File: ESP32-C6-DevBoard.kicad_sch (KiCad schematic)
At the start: 44 parts, among them J1 USB_C_Receptacle_USB2.0_16P, J2 Conn_01x10_Pin, J3 Conn_01x10_Pin, J4 USB_C_Receptacle_USB2.0_16P, Q1 BC847, Q2 BC847, SW1 SW_Push_Dual, SW2 SW_Push_Dual, U1 ESP32-C6-MINI-1, U2 CP2104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

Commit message: First version done without autorouter.
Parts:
- removed J2, J3: Conn_01x10_Pin, Connector_PinHeader_2.54mm:PinHeader_1x10_P2.54mm_Vertical, symbol Connector:Conn_01x10_Pin
- removed SW1, SW2: SW_Push_Dual, TS04_66_55_BK_260_SMT:SW_TS04-66-55-BK-260-SMT, symbol Switch:SW_Push_Dual
- removed U4, U5: USBLC6-2SC6, Package_TO_SOT_SMD:SOT-23-6, symbol Power_Protection:USBLC6-2SC6
- added D10, D11, D12, D6, D8, D9: SD05_SOD323, Diode_SMD:D_SOD-323, symbol Diode:SD05_SOD323
- added J2: Conn_01x02_Pin, Connector_PinHeader_2.54mm:PinHeader_1x02_P2.54mm_Vertical, symbol Connector:Conn_01x02_Pin
- added J5, J6: Conn_01x16_Pin, Connector_PinHeader_2.54mm:PinHeader_1x16_P2.54mm_Vertical, symbol Connector:Conn_01x16_Pin
- added S1, S2: TS-1088-AR02016, TS-1088-AR02016:SW_TS-1088-AR02016, symbol TS-1088-AR02016:TS-1088-AR02016
- C5: value 0.1uF -> 1.0uF
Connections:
- net CHIP_PU: now also S1.2
- net EIO0: now also S2.2
- net EIO1: now also J6.4 (Pin_4)
- net EIO14: now also J5.9 (Pin_9)
- net EIO15: now also J5.10 (Pin_10)
- net EIO18: now also J5.11 (Pin_11)
- net EIO19: now also J5.12 (Pin_12)
- net EIO2: now also J6.14 (Pin_14)
- net EIO20: now also J5.13 (Pin_13)
- net EIO21: now also J5.14 (Pin_14)
- net EIO22: now also J5.15 (Pin_15)
- net EIO23: now also J5.16 (Pin_16)
- net EIO3: now also J6.7 (Pin_7)
- net EIO4: now also J6.6 (Pin_6)
- net EIO5: now also J6.5 (Pin_5)
- net EIO6: now also J5.7 (Pin_7)
- net EIO7: now also J5.8 (Pin_8)
- net GND: now also D10.1 (A1), D11.1 (A1), D12.1 (A1), D6.1 (A1), D8.1 (A1), D9.1 (A1), J6.1 (Pin_1), S1.1, S2.1
- net USB1_N: now also J1.A7 (D-), J1.B7 (D-), D11.2 (A2)
- net USB1_P: now also J1.A6 (D+), J1.B6 (D+), D12.2 (A2)
- net USB2_N: now also J4.A7 (D-), J4.B7 (D-), D9.2 (A2)
- net USB2_P: now also J4.A6 (D+), J4.B6 (D+), D8.2 (A2)
- net DTR: now reaches Q2.3 (C), R11.2, U2.23 (~{DTR})
- net RTS: now reaches Q1.3 (C), R14.1, U2.19 (~{RTS})
- net 3V3 renamed PWR_3V3
- net PWR_3V3: now also J2.1 (Pin_1), J6.3 (Pin_3); no longer C2.1, R3.1, R5.1, U3.1 (OUT)
- net USB1_VBUS renamed PWR_USB1_VBUS
- net PWR_USB1_VBUS: now also D10.2 (A2)
- net USB2_VBUS renamed PWR_USB2_VBUS
- net PWR_USB2_VBUS: now also D6.2 (A2)
- net USB_5V renamed PWR_5V
- net PWR_5V: now also J6.2 (Pin_2)
- new net: C2.1, J2.2 (Pin_2), R3.1, R5.1, U3.1 (OUT)
- no-connect marks 14 -> 29
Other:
- note removed: "Pin grid"
- moved on the sheet: D3

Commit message: Updated silk screen and corrected component error
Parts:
- C1, C2, C7, C8: Part_No TORCH CT4G-1206-X5R-16V-10μF-K -> Samsung Electro-Mechanics CL10A106MA8NRNC
- C5: Part_No 0603B104K500NT -> Samsung Electro-Mechanics CL10A105KB8NNNC
- D10, D11, D12, D6, D8, D9: Part_No (none) -> MDD(Microdiode Semiconductor) SD05
- J2: Part_No (none) -> Ckmtw(Shenzhen Cankemeng) B-2100S02P-A110
- J5, J6: Part_No (none) -> HanElectricity 2541WV-16P
- S1, S2: Part_No (none) -> XUNPU TS-1088-AR02016

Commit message: Updated BOM
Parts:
- C1, C2, C7, C8: LCSC Part Name (none) -> C96446
- C3: LCSC Part Name (none) -> C19666
- C4, C6, C9: LCSC Part Name (none) -> C30926; Part_No 0603B104K500NT -> FH (Guangdong Fenghua Advanced Tech) 0603B104K500NT
- C5: LCSC Part Name (none) -> C15849
- D1: LCSC Part Name (none) -> C125123
- D10, D11, D12, D6, D8, D9: LCSC Part Name (none) -> C502527
- D2, D3: LCSC Part Name (none) -> C191023
- D4: LCSC Part Name (none) -> C125103
- D5, D7: LCSC Part Name (none) -> C12065
- J1, J4: LCSC Part Name (none) -> C2765186
- J2: LCSC Part Name (none) -> C124375
- J5, J6: LCSC Part Name (none) -> C25503134
- Q1, Q2: LCSC Part Name (none) -> C57668
- R1, R2, R7, R8: LCSC Part Name (none) -> C23186
- R10, R13, R15, R17, R5, R9: LCSC Part Name (none) -> C23197
- R11, R14, R6: LCSC Part Name (none) -> C25804
- R12: LCSC Part Name (none) -> C23179
- R3: LCSC Part Name (none) -> C22935
- R4: LCSC Part Name (none) -> C25811
- S1, S2: LCSC Part Name (none) -> C720477
- U1: LCSC Part Name (none) -> C5736265
- U2: LCSC Part Name (none) -> C47742
- U3: LCSC Part Name (none) -> C2876308
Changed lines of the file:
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@@
 			)
 		)
-		(property "LCSC Part Name" ""
+		(property "LCSC Part Name" "C125103"
 			(at 66.04 36.83 0)
 			(effects
@@
 			)
 		)
-		(property "LCSC Part Name" ""
+		(property "LCSC Part Name" "C12065"
 			(at 38.1 168.91 0)
 			(effects
@@
 			)
 		)
-		(property "LCSC Part Name" ""
+		(property "LCSC Part Name" "C720477"
 			(at 295.91 64.77 0)
 			(effects
@@
 			)
 		)
-		(property "LCSC Part Name" ""
+		(property "LCSC Part Name" "C25804"
 			(at 227.33 48.26 0)
 			(effects
@@
 			)
 		)
-		(property "Part_No" "0603B104K500NT"
+		(property "Part_No" "FH (Guangdong Fenghua Advanced Tech) 0603B104K500NT"
 			(at 368.3 26.67 0)
 			(effects
@@
 			)
 		)
-		(property "LCSC Part Name" ""
+		(property "LCSC Part Name" "C30926"
 			(at 368.3 26.67 0)
 			(effects
@@
 			)
 		)
-		(property "LCSC Part Name" ""
+		(property "LCSC Part Name" "C502527"
 			(at 63.5 54.61 0)
 			(effects
@@
 			)
 		)
-		(property "LCSC Part Name" ""
+		(property "LCSC Part Name" "C125123"
 			(at 91.44 168.91 0)
 			(effects
@@
 			)
 		)
-		(property "LCSC Part Name" ""
+		(property "LCSC Part Name" "C23197"
 			(at 195.58 38.1 0)
 			(effects
@@
 			)
 		)
-		(property "LCSC Part Name" ""
+		(property "LCSC Part Name" "C720477"
 			(at 295.91 43.18 0)
 			(effects
@@
 			)
 		)
-		(property "LCSC Part Name" ""
+		(property "LCSC Part Name" "C15849"
 			(at 303.53 46.99 0)
 			(effects
@@
 			)
 		)
-		(property "Part_No" "0603B104K500NT"
+		(property "Part_No" "FH (Guangdong Fenghua Advanced Tech) 0603B104K500NT"
 			(at 316.23 69.85 0)
 			(effects
@@
 			)
 		)
-		(property "LCSC Part Name" ""
+		(property "LCSC Part Name" "C30926"
 			(at 316.23 69.85 0)
 			(effects
@@
 			)
 		)
-		(property "LCSC Part Name" ""
+		(property "LCSC Part Name" "C25804"
 			(at 303.53 26.67 0)
 			(effects
@@
 			)
 		)
-		(property "LCSC Part Name" ""
+		(property "LCSC Part Name" "C96446"
 			(at 78.74 163.83 0)
 			(effects
@@
 			)
 		)
-		(property "LCSC Part Name" ""
+		(property "LCSC Part Name" "C57668"
 			(at 234.95 72.39 0)
 			(effects
@@
 			)
 		)
-		(property "LCSC Part Name" ""
+		(property "LCSC Part Name" "C22935"
 			(at 66.04 161.29 0)
 			(effects
@@
 			)
 		)
-		(property "LCSC Part Name" ""
+		(property "LCSC Part Name" "C23197"
 			(at 66.04 29.21 0)
 			(effects
@@
 			)
 		)
-		(property "LCSC Part Name" ""
+		(property "LCSC Part Name" "C5736265"
 			(at 350.52 63.5 0)
 			(effects
@@
 			)
 		)
-		(property "LCSC Part Name" ""
+		(property "LCSC Part Name" "C502527"
 			(at 74.93 38.1 0)
 			(effects
@@
 			)
 		)
-		(property "LCSC Part Name" ""
+		(property "LCSC Part Name" "C23186"
 			(at 58.42 36.83 0)
 			(effects
@@
 			)
 		)
-		(property "LCSC Part Name" ""
+		(property "LCSC Part Name" "C23197"
 			(at 38.1 161.29 0)
 			(effects
@@
 			)
 		)
-		(property "LCSC Part Name" ""
+		(property "LCSC Part Name" "C57668"
 			(at 237.49 48.26 0)
 			(effects
@@
 			)
 		)
-		(property "LCSC Part Name" ""
+		(property "LCSC Part Name" "C2876308"
 			(at 48.26 160.02 0)
 			(effects
@@
 			)
 		)
-		(property "LCSC Part Name" ""
+		(property "LCSC Part Name" "C124375"
 			(at 97.79 152.4 0)
 			(effects
@@
 			)
 		)
-		(property "LCSC Part Name" ""
+		(property "LCSC Part Name" "C23197"
 			(at 195.58 35.56 0)
 			(effects
@@
 			)
 		)
-		(property "LCSC Part Name" ""
+		(property "LCSC Part Name" "C12065"
 			(at 63.5 100.33 0)
 			(effects
@@
 			)
 		)
-		(property "LCSC Part Name" ""
+		(property "LCSC Part Name" "C191023"
 			(at 78.74 88.9 0)
 			(effects
@@
 			)
 		)
-		(property "LCSC Part Name" ""
+		(property "LCSC Part Name" "C502527"
 			(at 74.93 102.87 0)
 			(effects
@@
 			)
 		)
-		(property "Part_No" "0603B104K500NT"
+		(property "Part_No" "FH (Guangdong Fenghua Advanced Tech) 0603B104K500NT"
 			(at 144.78 30.48 0)
 			(effects
@@
 			)
 		)
-		(property "LCSC Part Name" ""
+		(property "LCSC Part Name" "C30926"
 			(at 144.78 30.48 0)
 			(effects
@@
 			)
 		)
-		(property "LCSC Part Name" ""
+		(property "LCSC Part Name" "C2765186"
 			(at 39.37 46.99 0)
 			(effects
@@
 			)
 		)
-		(property "LCSC Part Name" ""
+		(property "LCSC Part Name" "C502527"
 			(at 68.58 120.65 0)
 			(effects
@@
 			)
 		)
-		(property "LCSC Part Name" ""
+		(property "LCSC Part Name" "C23197"
 			(at 91.44 162.56 0)
 			(effects
@@
 			)
 		)
-		(property "LCSC Part Name" ""
+		(property "LCSC Part Name" "C25811"
 			(at 66.04 168.91 0)
 			(effects
@@
 			)
 		)
-		(property "LCSC Part Name" ""
+		(property "LCSC Part Name" "C23197"
 			(at 63.5 92.71 0)
 			(effects
@@
 			)
 		)
-		(property "LCSC Part Name" ""
+		(property "LCSC Part Name" "C23186"
 			(at 58.42 40.64 0)
 			(effects
@@
 			)
 		)
-		(property "LCSC Part Name" ""
+		(property "LCSC Part Name" "C96446"
 			(at 356.87 26.67 0)
 			(effects
@@
 			)
 		)
-		(property "LCSC Part Name" ""
+		(property "LCSC Part Name" "C2765186"
 			(at 33.02 113.03 0)
 			(effects
@@
 			)
 		)
-		(property "LCSC Part Name" ""
+		(property "LCSC Part Name" "C502527"
 			(at 59.69 120.65 0)
 			(effects
@@
 			)
 		)
-		(property "LCSC Part Name" ""
+		(property "LCSC Part Name" "C23186"
 			(at 57.15 105.41 0)
 			(effects
@@
 			)
 		)
-		(property "LCSC Part Name" ""
+		(property "LCSC Part Name" "C23179"
 			(at 160.02 31.75 0)
 			(effects
@@
 			)
 		)
-		(property "LCSC Part Name" ""
+		(property "LCSC Part Name" "C191023"
 			(at 80.01 31.75 0)
 			(effects
@@
 			)
 		)
-		(property "LCSC Part Name" ""
+		(property "LCSC Part Name" "C19666"
 			(at 157.48 82.55 0)
 			(effects
@@
 			)
 		)
-		(property "LCSC Part Name" ""
+		(property "LCSC Part Name" "C47742"
 			(at 176.53 58.42 0)
 			(effects
@@
 			)
 		)
-		(property "LCSC Part Name" ""
+		(property "LCSC Part Name" "C96446"
 			(at 152.4 30.48 0)
 			(effects
@@
 			)
 		)
-		(property "LCSC Part Name" ""
+		(property "LCSC Part Name" "C96446"
 			(at 33.02 163.83 0)
 			(effects
@@
 			)
 		)
-		(property "LCSC Part Name" ""
+		(property "LCSC Part Name" "C25804"
 			(at 226.06 72.39 0)
 			(effects
@@
 			)
 		)
-		(property "LCSC Part Name" ""
+		(property "LCSC Part Name" "C25503134"
 			(at 203.2 144.78 0)
 			(effects
@@
 			)
 		)
-		(property "LCSC Part Name" ""
+		(property "LCSC Part Name" "C25503134"
 			(at 228.6 144.78 0)
 			(effects
@@
 			)
 		)
-		(property "LCSC Part Name" ""
+		(property "LCSC Part Name" "C23186"
 			(at 57.15 100.33 0)
 			(effects
@@
 			)
 		)
-		(property "LCSC Part Name" ""
+		(property "LCSC Part Name" "C502527"
 			(at 73.66 54.61 0)
 			(effects

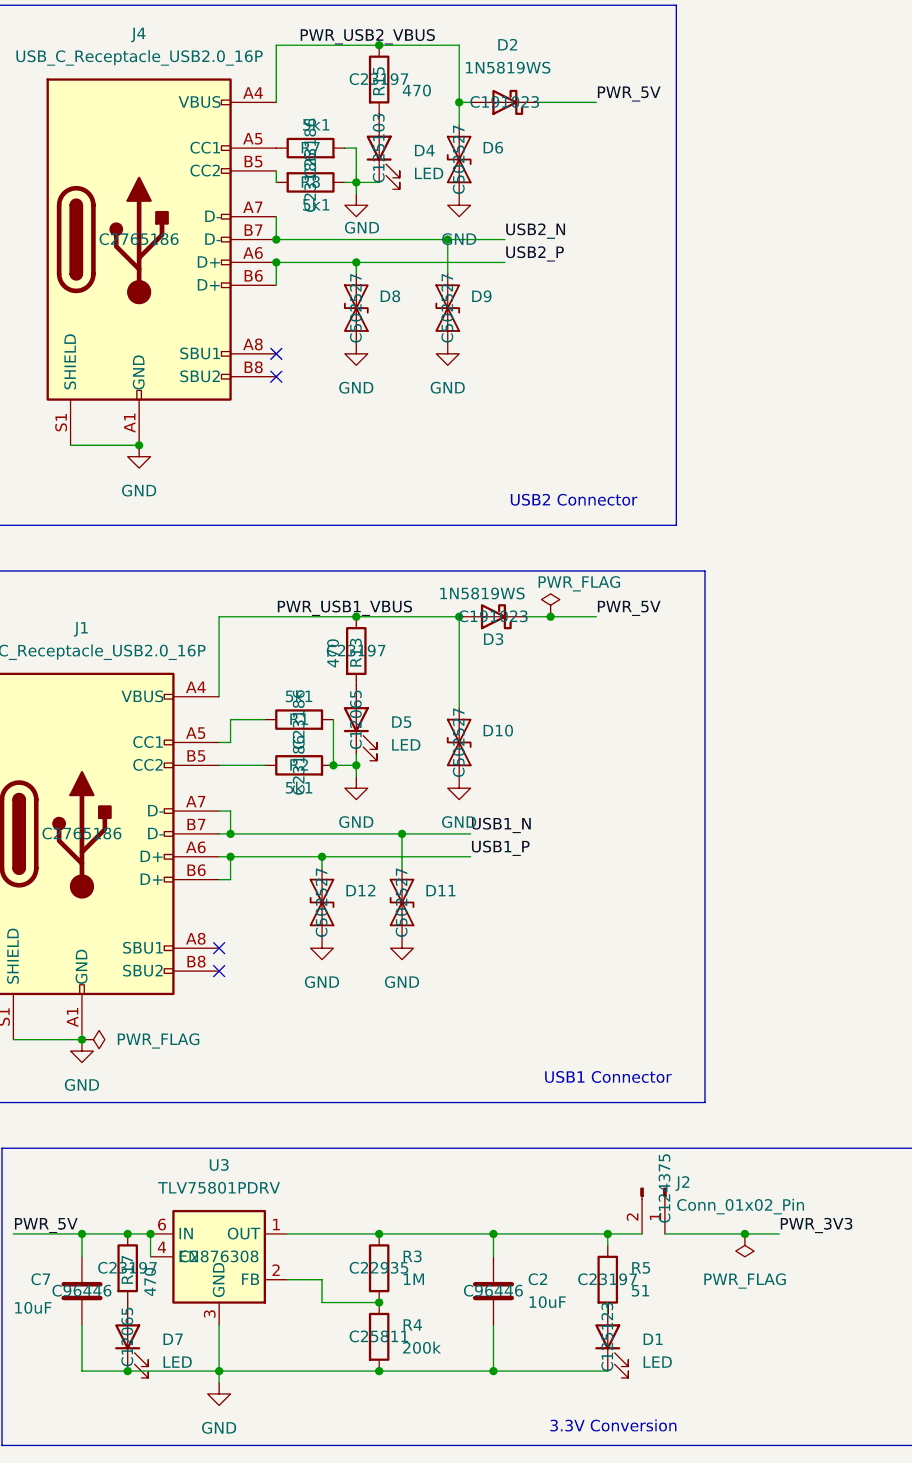
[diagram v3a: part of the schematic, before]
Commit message: Updated BOM using Buoni kicad-jlcpcb-tools
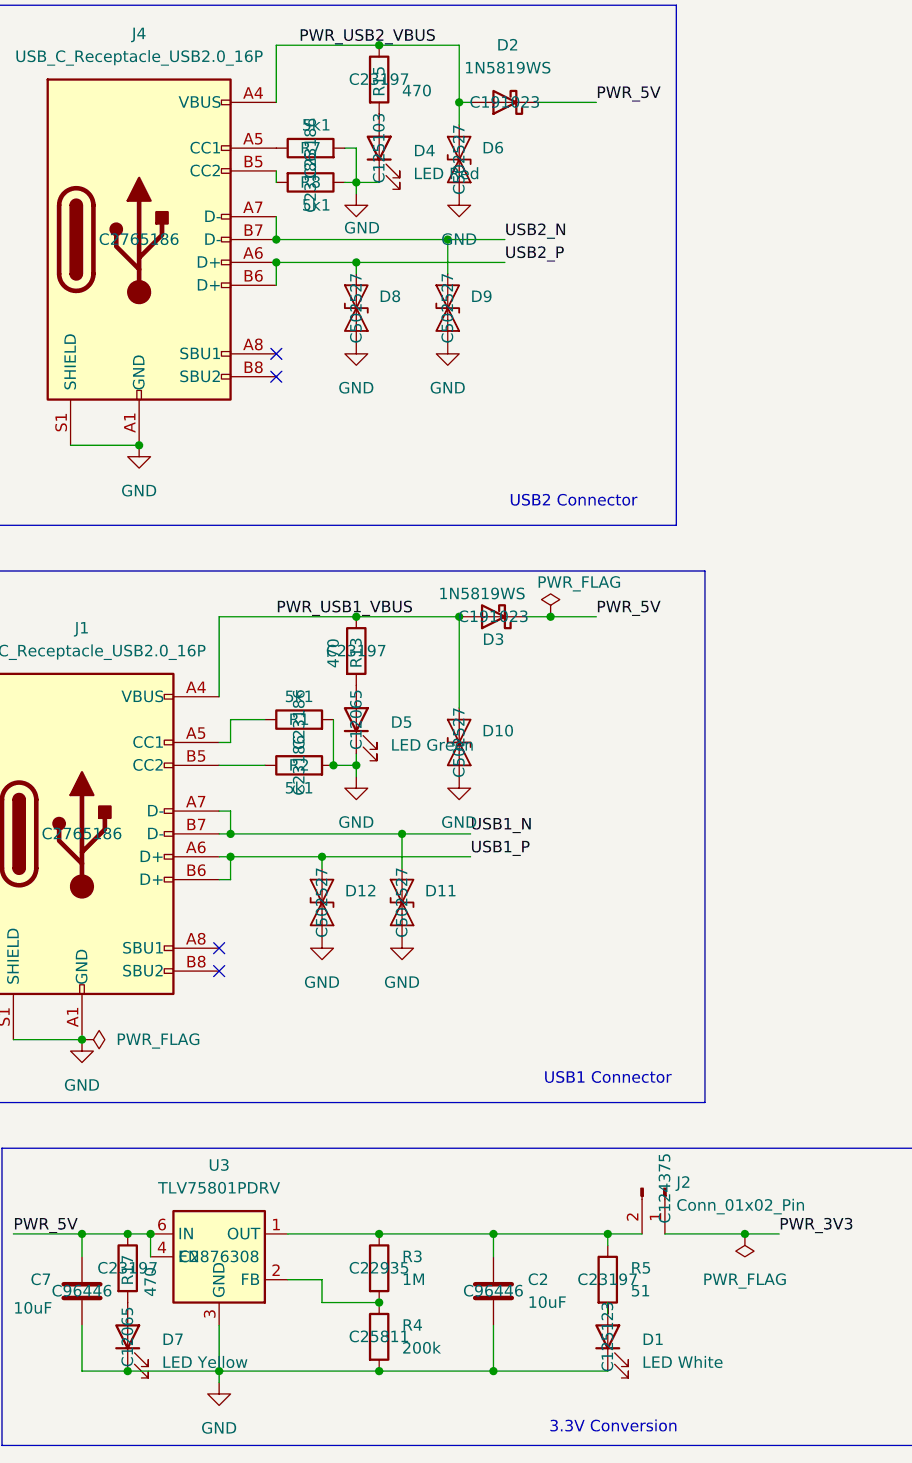
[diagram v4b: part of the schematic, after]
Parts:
- C1, C2, C7, C8: LCSC (none) -> C96446
- C3: LCSC (none) -> C19666
- C4, C6, C9: LCSC (none) -> C1590
- C5: LCSC (none) -> C1592
- D1: value LED -> LED White; LCSC (none) -> C2290
- D10, D11, D12, D6, D8, D9: LCSC (none) -> C502527
- D2, D3: LCSC (none) -> C191023
- D4: value LED -> LED Red; LCSC (none) -> C2286
- D5: value LED -> LED Green; LCSC (none) -> C916074
- D7: value LED -> LED Yellow; LCSC (none) -> C72038
- J1, J4: LCSC (none) -> C2765186
- J2: LCSC (none) -> C706874
- J5, J6: LCSC (none) -> C725948
- Q1, Q2: LCSC (none) -> C57668
- R1, R2, R7, R8: LCSC (none) -> C23186
- R10, R13, R15, R17, R9: LCSC (none) -> C23179
- R11, R14, R6: LCSC (none) -> C25804
- R12: LCSC (none) -> C21190
- R3: LCSC (none) -> C22935
- R4: LCSC (none) -> C25811
- R5: LCSC (none) -> C23197
- S1, S2: LCSC (none) -> C720477
- U1: LCSC (none) -> C5736265
- U2: LCSC (none) -> C47742
- U3: LCSC (none) -> C2876308
